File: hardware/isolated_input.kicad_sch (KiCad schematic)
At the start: 3 parts, among them U2 LTV-817S

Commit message: finalize revision of schematic
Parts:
- renumbered R1 to R2, R7 to R3, U2 to U3
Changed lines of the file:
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@@
 		(dnp no)
 		(fields_autoplaced yes)
-		(property "Reference" "R1"
+		(property "Reference" "R2"
 			(at 139.7 123.1899 0)
 			(effects
@@
 			(project "BREAD_Slice"
 				(path "/66043bca-a260-4915-9fce-8a51d324c687/237ecdf4-0ec6-4779-9712-21a21e3b44fb"
+					(reference "R4")
+					(unit 1)
+				)
+				(path "/66043bca-a260-4915-9fce-8a51d324c687/4214154c-51ea-452d-92fc-56119205d2c3"
+					(reference "R8")
+					(unit 1)
+				)
+				(path "/66043bca-a260-4915-9fce-8a51d324c687/b64880f2-481d-450b-a976-c6882ac5d67f"
+					(reference "R6")
+					(unit 1)
+				)
+				(path "/66043bca-a260-4915-9fce-8a51d324c687/f4bc6ab1-c08e-4bad-8836-4e168b2fbdc6"
 					(reference "R2")
-					(unit 1)
-				)
-				(path "/66043bca-a260-4915-9fce-8a51d324c687/4214154c-51ea-452d-92fc-56119205d2c3"
-					(reference "R6")
-					(unit 1)
-				)
-				(path "/66043bca-a260-4915-9fce-8a51d324c687/b64880f2-481d-450b-a976-c6882ac5d67f"
-					(reference "R4")
-					(unit 1)
-				)
-				(path "/66043bca-a260-4915-9fce-8a51d324c687/f4bc6ab1-c08e-4bad-8836-4e168b2fbdc6"
-					(reference "R1")
 					(unit 1)
 				)
@@
 		(dnp no)
 		(fields_autoplaced yes)
-		(property "Reference" "R7"
+		(property "Reference" "R3"
 			(at 166.37 109.22 90)
 			(effects
@@
 			(project "BREAD_Slice"
 				(path "/66043bca-a260-4915-9fce-8a51d324c687/237ecdf4-0ec6-4779-9712-21a21e3b44fb"
+					(reference "R5")
+					(unit 1)
+				)
+				(path "/66043bca-a260-4915-9fce-8a51d324c687/4214154c-51ea-452d-92fc-56119205d2c3"
+					(reference "R9")
+					(unit 1)
+				)
+				(path "/66043bca-a260-4915-9fce-8a51d324c687/b64880f2-481d-450b-a976-c6882ac5d67f"
+					(reference "R7")
+					(unit 1)
+				)
+				(path "/66043bca-a260-4915-9fce-8a51d324c687/f4bc6ab1-c08e-4bad-8836-4e168b2fbdc6"
 					(reference "R3")
-					(unit 1)
-				)
-				(path "/66043bca-a260-4915-9fce-8a51d324c687/4214154c-51ea-452d-92fc-56119205d2c3"
-					(reference "R8")
-					(unit 1)
-				)
-				(path "/66043bca-a260-4915-9fce-8a51d324c687/b64880f2-481d-450b-a976-c6882ac5d67f"
-					(reference "R5")
-					(unit 1)
-				)
-				(path "/66043bca-a260-4915-9fce-8a51d324c687/f4bc6ab1-c08e-4bad-8836-4e168b2fbdc6"
-					(reference "R7")
 					(unit 1)
 				)
@@
 		(on_board yes)
 		(dnp no)
-		(property "Reference" "U2"
+		(property "Reference" "U3"
 			(at 147.32 110.744 0)
 			(effects
@@
 			(project "BREAD_Slice"
 				(path "/66043bca-a260-4915-9fce-8a51d324c687/237ecdf4-0ec6-4779-9712-21a21e3b44fb"
+					(reference "U4")
+					(unit 1)
+				)
+				(path "/66043bca-a260-4915-9fce-8a51d324c687/4214154c-51ea-452d-92fc-56119205d2c3"
+					(reference "U6")
+					(unit 1)
+				)
+				(path "/66043bca-a260-4915-9fce-8a51d324c687/b64880f2-481d-450b-a976-c6882ac5d67f"
+					(reference "U5")
+					(unit 1)
+				)
+				(path "/66043bca-a260-4915-9fce-8a51d324c687/f4bc6ab1-c08e-4bad-8836-4e168b2fbdc6"
 					(reference "U3")
 					(unit 1)
 				)
-				(path "/66043bca-a260-4915-9fce-8a51d324c687/4214154c-51ea-452d-92fc-56119205d2c3"
-					(reference "U5")
-					(unit 1)
-				)
-				(path "/66043bca-a260-4915-9fce-8a51d324c687/b64880f2-481d-450b-a976-c6882ac5d67f"
-					(reference "U4")
-					(unit 1)
-				)
-				(path "/66043bca-a260-4915-9fce-8a51d324c687/f4bc6ab1-c08e-4bad-8836-4e168b2fbdc6"
-					(reference "U2")
-					(unit 1)
-				)

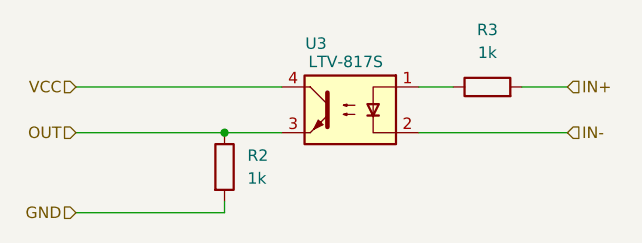
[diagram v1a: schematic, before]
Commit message: revision of symbol attachment and clear out old layout and start new; kml-custom to kmlib-local
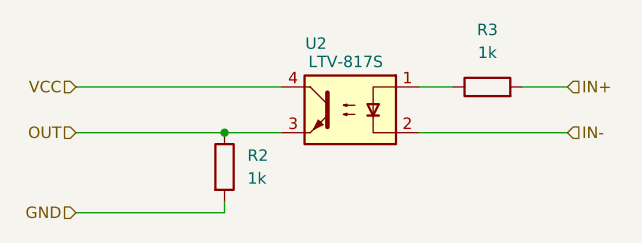
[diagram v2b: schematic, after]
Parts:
- renumbered U3 to U2
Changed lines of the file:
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@@
 		(on_board yes)
 		(dnp no)
-		(property "Reference" "U3"
+		(property "Reference" "U2"
 			(at 147.32 110.744 0)
 			(effects
@@
 			(project "BREAD_Slice"
 				(path "/66043bca-a260-4915-9fce-8a51d324c687/237ecdf4-0ec6-4779-9712-21a21e3b44fb"
+					(reference "U3")
+					(unit 1)
+				)
+				(path "/66043bca-a260-4915-9fce-8a51d324c687/4214154c-51ea-452d-92fc-56119205d2c3"
+					(reference "U5")
+					(unit 1)
+				)
+				(path "/66043bca-a260-4915-9fce-8a51d324c687/b64880f2-481d-450b-a976-c6882ac5d67f"
 					(reference "U4")
 					(unit 1)
 				)
-				(path "/66043bca-a260-4915-9fce-8a51d324c687/4214154c-51ea-452d-92fc-56119205d2c3"
-					(reference "U6")
+				(path "/66043bca-a260-4915-9fce-8a51d324c687/f4bc6ab1-c08e-4bad-8836-4e168b2fbdc6"
+					(reference "U2")
 					(unit 1)
 				)
-				(path "/66043bca-a260-4915-9fce-8a51d324c687/b64880f2-481d-450b-a976-c6882ac5d67f"
-					(reference "U5")
-					(unit 1)
-				)
-				(path "/66043bca-a260-4915-9fce-8a51d324c687/f4bc6ab1-c08e-4bad-8836-4e168b2fbdc6"
-					(reference "U3")
-					(unit 1)
-				)
